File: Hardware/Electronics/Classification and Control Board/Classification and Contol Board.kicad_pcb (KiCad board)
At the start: 2 copper layers, 1 part, among them U1 STM32F407VETx

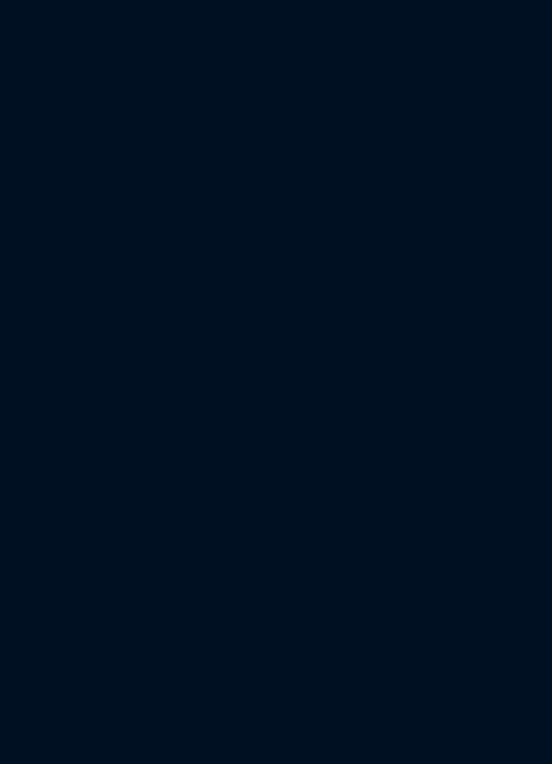
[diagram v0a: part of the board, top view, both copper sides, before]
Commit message: Added SWD programming header
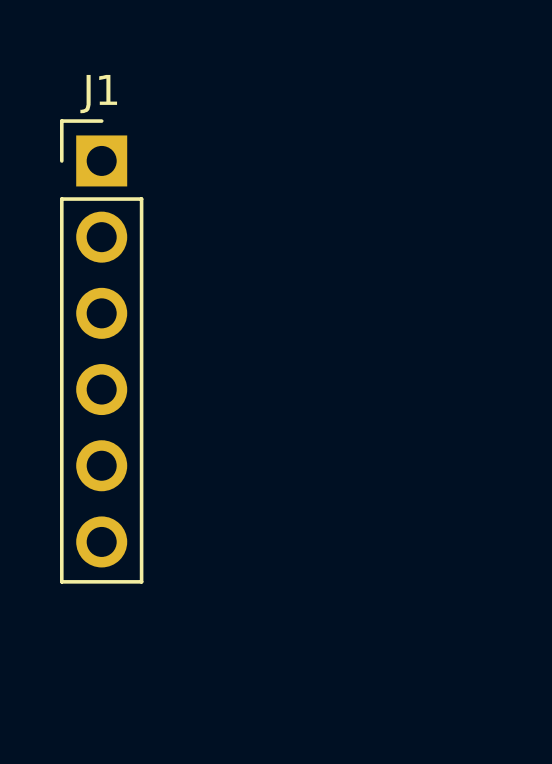
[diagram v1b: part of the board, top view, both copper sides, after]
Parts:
- added J1: Conn_01x06_Male, Connector_PinHeader_2.54mm:PinHeader_1x06_P2.54mm_Vertical, F.Cu at (100.2, 56.7)
- U1: value STM32F407VETx -> STM32F407VGTx
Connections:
- U1 pad 14: Net-(U1-Pad14) -> /NRST
- U1 pad 76: Net-(U1-Pad76) -> /SWCLK
- U1 pad 89: Net-(U1-Pad89) -> /SWO

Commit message: removed some decoupling, started layout
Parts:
- added C1: 100u, Capacitor_SMD:CP_Elec_6.3x7.7, F.Cu at (274.9, 66.3)
- added C10: 100n, Capacitor_SMD:C_0603_1608Metric, F.Cu at (242.5, 34.6)
- added C11: 10n, Capacitor_SMD:C_0603_1608Metric, F.Cu at (244.1, 34.6)
- added C12: 10n, Capacitor_SMD:C_0603_1608Metric, F.Cu at (245.7, 34.6)
- added C13: 0.1u, Capacitor_SMD:C_0603_1608Metric, F.Cu at (249.5, 49.2)
- added C15: 4.7u, Capacitor_SMD:C_0603_1608Metric, F.Cu at (272.9, 56.7)
- added C16: 100n, Capacitor_SMD:C_0603_1608Metric, F.Cu at (240.9, 41.4)
- added C17: 100n, Capacitor_SMD:C_0603_1608Metric, F.Cu at (242.5, 41.4)
- added C18: 10n, Capacitor_SMD:C_0603_1608Metric, F.Cu at (244.0, 41.4)
- added C19: 10n, Capacitor_SMD:C_0603_1608Metric, F.Cu at (245.6, 41.4)
- added C2: 100n, Capacitor_SMD:C_0603_1608Metric, F.Cu at (244.8, 27.1)
- added C20: 10n, Capacitor_SMD:C_0603_1608Metric, F.Cu at (272.9, 55.1)
- added C21: 100n, Capacitor_SMD:C_0603_1608Metric, F.Cu at (255.7, 49.2)
- added C22: 100n, Capacitor_SMD:C_0603_1608Metric, F.Cu at (254.2, 49.2)
- added C23: 10n, Capacitor_SMD:C_0603_1608Metric, F.Cu at (252.6, 49.2)
- added C24: 10n, Capacitor_SMD:C_0603_1608Metric, F.Cu at (251.1, 49.2)
- added C25: 1n, Capacitor_SMD:C_0603_1608Metric, F.Cu at (272.9, 53.6)
- added C26: 100n, Capacitor_SMD:C_0603_1608Metric, F.Cu at (263.9, 52.8)
- added C27: 100n, Capacitor_SMD:C_0603_1608Metric, F.Cu at (263.9, 51.2)
- added C28: 10n, Capacitor_SMD:C_0603_1608Metric, F.Cu at (263.9, 49.7)
- added C29: 10n, Capacitor_SMD:C_0603_1608Metric, F.Cu at (263.9, 48.1)
- added C3: 100n, Capacitor_SMD:C_0603_1608Metric, F.Cu at (244.8, 28.8)
- added C30: 100n, Capacitor_SMD:C_0603_1608Metric, F.Cu at (266.7, 27.2)
- added C31: 100n, Capacitor_SMD:C_0603_1608Metric, F.Cu at (266.7, 28.7)
- added C32: 10n, Capacitor_SMD:C_0603_1608Metric, F.Cu at (266.7, 30.3)
- added C33: 10n, Capacitor_SMD:C_0603_1608Metric, F.Cu at (266.7, 31.8)
- added C34: 10n, Capacitor_SMD:C_0603_1608Metric, F.Cu at (245.2, 50.2)
- added C35: 100n, Capacitor_SMD:C_0603_1608Metric, F.Cu at (249.2, 24.0)
- added C36: 100n, Capacitor_SMD:C_0603_1608Metric, F.Cu at (249.2, 25.6)
- added C37: 10n, Capacitor_SMD:C_0603_1608Metric, F.Cu at (249.2, 27.1)
- added C38: 10n, Capacitor_SMD:C_0603_1608Metric, F.Cu at (249.2, 28.6)
- added C39: 100n, Capacitor_SMD:C_0603_1608Metric, F.Cu at (245.2, 48.6)
- added C4: 10n, Capacitor_SMD:C_0603_1608Metric, F.Cu at (245.0, 32.0)
- added C40: 1n, Capacitor_SMD:C_0603_1608Metric, F.Cu at (270.6, 42.7)
- added C41: 1u, Capacitor_SMD:C_0603_1608Metric, F.Cu at (245.2, 47.1)
- added C46: 10n, Capacitor_SMD:C_0603_1608Metric, F.Cu at (270.6, 41.2)
- added C47: 4.7u, Capacitor_SMD:C_0603_1608Metric, F.Cu at (270.6, 39.6)
- added C48: 10u, Capacitor_SMD:CP_Elec_4x5.4, F.Cu at (271.6, 36.2)
- added C49: 2.2u, Capacitor_SMD:C_0603_1608Metric, F.Cu at (261.6, 49.0)
- added C5: 10n, Capacitor_SMD:C_0603_1608Metric, F.Cu at (244.8, 30.4)
- added C50: 1u, Capacitor_SMD:C_0603_1608Metric, F.Cu at (244.1, 44.5)
- added C51: 2.2u, Capacitor_SMD:C_0603_1608Metric, F.Cu at (266.7, 33.4)
- added C52: 10n, Capacitor_SMD:C_0603_1608Metric, F.Cu at (245.7, 44.5)
- added C53: 100u, Capacitor_SMD:CP_Elec_6.3x7.7, F.Cu at (244.3, 94.6)
- added C54: 100u, Capacitor_SMD:CP_Elec_6.3x7.7, F.Cu at (251.8, 94.5)
- added C55: 10u, Capacitor_SMD:CP_Elec_4x5.4, F.Cu at (258.0, 95.8)
- added C56: 10u, Capacitor_SMD:CP_Elec_4x5.4, F.Cu at (262.9, 95.7)
- added C57: 4.7u, Capacitor_SMD:C_0603_1608Metric, F.Cu at (270.7, 97.5)
- added C60: 4.7u, Capacitor_SMD:C_0603_1608Metric, F.Cu at (37.7, 15.9)
- added C61: 100n, Capacitor_SMD:C_0603_1608Metric, F.Cu at (49.2, 12.4)
- added C62: 100n, Capacitor_SMD:C_0603_1608Metric, F.Cu at (39.2, 15.9)
- added C63: 10n, Capacitor_SMD:C_0603_1608Metric, F.Cu at (47.7, 12.4)
- added C64: 10n, Capacitor_SMD:C_0603_1608Metric, F.Cu at (40.8, 15.9)
- added C65: 10n, Capacitor_SMD:C_0603_1608Metric, F.Cu at (47.7, 9.29)
- added C67: 100n, Capacitor_SMD:C_0603_1608Metric, F.Cu at (49.2, 9.30)
- added C68: 4.7u, Capacitor_SMD:C_0603_1608Metric, F.Cu at (40.8, 20.1)
- added C7: 10u, Capacitor_SMD:CP_Elec_4x5.4, F.Cu at (273.9, 60.0)
- added C70: 100n, Capacitor_SMD:C_0603_1608Metric, F.Cu at (39.3, 20.1)
- added C71: 10n, Capacitor_SMD:C_0603_1608Metric, F.Cu at (37.7, 20.1)
- added C9: 100n, Capacitor_SMD:C_0603_1608Metric, F.Cu at (240.9, 34.6)
- added D1: LTST-C171TBKT, LED_SMD:LED_0805_2012Metric, F.Cu at (-17.4, -14.9)
- added D2: LO R976-PS-1, LED_SMD:LED_0805_2012Metric, F.Cu at (17.1, -25.7)
- added D3: 10V, Diode_SMD:D_SMA, F.Cu at (237.2, 96.6)
- added D4: LED, LED_SMD:LED_0603_1608Metric, F.Cu at (-64.0, -19.9)
- added D5: LED, LED_SMD:LED_0603_1608Metric, F.Cu at (-61.0, -19.9)
- added D6: LED, LED_SMD:LED_0603_1608Metric, F.Cu at (-23.2, -42.0)
- added F1: Fuse, Resistor_THT:R_Axial_Power_L20.0mm_W6.4mm_P25.40mm, F.Cu at (235.2, 85.5)
- added J10: USB_B_Mini, Connector_USB:USB_Micro-B_Wuerth_629105150521, F.Cu at (-76.6, 8.15)
- added J2: Barrel_Jack, Connector_BarrelJack:BarrelJack_CUI_PJ-063AH_Horizontal, F.Cu at (227.5, 85.8)
- added J3: Thumb, Connector_PinHeader_2.54mm:PinHeader_1x03_P2.54mm_Horizontal, F.Cu at (106.2, 92.0)
- added J4: Index, Connector_PinHeader_2.54mm:PinHeader_1x03_P2.54mm_Horizontal, F.Cu at (115.0, 92.0)
- added J5: Middle, Connector_PinHeader_2.54mm:PinHeader_1x03_P2.54mm_Horizontal, F.Cu at (123.7, 92.0)
- added J6: Ring, Connector_PinHeader_2.54mm:PinHeader_1x03_P2.54mm_Horizontal, F.Cu at (136.0, 92.4)
- added J7: Pinky, Connector_PinHeader_2.54mm:PinHeader_1x03_P2.54mm_Horizontal, F.Cu at (135.9, 101.4)
- added J8: Wrist, Connector_PinHeader_2.54mm:PinHeader_1x03_P2.54mm_Horizontal, F.Cu at (135.9, 110.1)
- added J9: HC05, Resonators:HC-05, F.Cu at (80.4, -68.8)
- added LOGO1: SparkerLogo, Sparker:NASA, F.Cu at (-95.3, -20.5)
- added LOGO2: UoNLogo, Sparker:UoN, F.Cu at (-93.0, -1.31)
- added MH1: MountingHole, MountingHole:MountingHole_2.7mm_M2.5, F.Cu at (-34.3, 7.48)
- added MH2: MountingHole, MountingHole:MountingHole_2.7mm_M2.5, F.Cu at (-40.2, 7.48)
- added MH3: MountingHole, MountingHole:MountingHole_2.7mm_M2.5, F.Cu at (-52.4, 8.02)
- added MH4: MountingHole, MountingHole:MountingHole_2.7mm_M2.5, F.Cu at (-46.2, 7.48)
- added Q1: SQ3425EV-T1_GE3, Package_TO_SOT_SMD:TSOT-23-6, F.Cu at (238.2, 92.9)
- added R1: 100k, Resistor_SMD:R_0603_1608Metric, F.Cu at (252.9, 22.5)
- added R10: 50m, Resistor_SMD:R_0603_1608Metric, F.Cu at (132.5, 103.9)
- added R11: 50m, Resistor_SMD:R_0603_1608Metric, F.Cu at (132.5, 112.7)
- added R12: 500k, Resistor_SMD:R_0603_1608Metric, F.Cu at (245.2, 53.3)
- added R13: 100k, Resistor_SMD:R_0603_1608Metric, F.Cu at (245.2, 51.8)
- added R14: 500k, Resistor_SMD:R_0603_1608Metric, F.Cu at (106.5, 94.8)
- added R15: 100k, Resistor_SMD:R_0603_1608Metric, F.Cu at (106.4, 96.4)
- added R16: 500k, Resistor_SMD:R_0603_1608Metric, F.Cu at (115.2, 94.7)
- added R17: 100k, Resistor_SMD:R_0603_1608Metric, F.Cu at (115.2, 96.3)
- added R18: 500k, Resistor_SMD:R_0603_1608Metric, F.Cu at (123.9, 94.7)
- added R19: 100k, Resistor_SMD:R_0603_1608Metric, F.Cu at (123.9, 96.2)
- added R2: 100k, Resistor_SMD:R_0603_1608Metric, F.Cu at (252.9, 20.9)
- added R20: 500k, Resistor_SMD:R_0603_1608Metric, F.Cu at (133.3, 92.7)
- added R21: 100k, Resistor_SMD:R_0603_1608Metric, F.Cu at (131.8, 92.7)
- added R22: 500k, Resistor_SMD:R_0603_1608Metric, F.Cu at (133.3, 101.6)
- added R23: 100k, Resistor_SMD:R_0603_1608Metric, F.Cu at (131.7, 101.6)
- added R24: 500k, Resistor_SMD:R_0603_1608Metric, F.Cu at (133.3, 110.4)
- added R25: 100k, Resistor_SMD:R_0603_1608Metric, F.Cu at (131.8, 110.4)
- added R26: 150, Resistor_SMD:R_0603_1608Metric, F.Cu at (-64.0, -17.0)
- added R27: 150, Resistor_SMD:R_0603_1608Metric, F.Cu at (-60.9, -23.1)
- added R28: 150, Resistor_SMD:R_0603_1608Metric, F.Cu at (-19.0, -41.8)
- added R4: 65R, Resistor_SMD:R_0603_1608Metric, F.Cu at (17.2, -28.4)
- added R5: 33k, Resistor_SMD:R_0603_1608Metric, F.Cu at (234.4, 93.2)
- added R6: 50m, Resistor_SMD:R_0603_1608Metric, F.Cu at (108.8, 95.6)
- added R7: 50m, Resistor_SMD:R_0603_1608Metric, F.Cu at (117.5, 95.5)
- added R8: 50m, Resistor_SMD:R_0603_1608Metric, F.Cu at (126.2, 95.5)
- added R9: 50m, Resistor_SMD:R_0603_1608Metric, F.Cu at (132.5, 95.0)
- added SW1: SW_Push, Switches:1825910-6, F.Cu at (235.0, 52.0)
- added SW2: SW_DIP_x02, Switches:DIP-Switch_01x02, F.Cu at (253.1, 25.0)
- added SW3: BT Enable, Switches:DIP-Switch_01x02, F.Cu at (32.8, 13.1)
- added U2: STM32F407VGTx, Package_QFP:LQFP-100_14x14mm_P0.5mm, F.Cu at (256.1, 38.4)
- added U3: MCP1755T-5002E_SOT223-5, Package_TO_SOT_SMD:SOT-223-6, F.Cu at (46.1, 18.0)
- added U4: FT232RL, Package_SO:SSOP-28_5.3x10.2mm_P0.65mm, F.Cu at (42.0, 7.48)
- added Y1: 12MHz, Resonators:CSTNE12M0GH5L000R0, F.Cu at (245.1, 38.2)
- J1: value Conn_01x06_Male -> SWD Header
- U1: value STM32F407VGTx -> LDL1117S33R; footprint Package_QFP:LQFP-100_14x14mm_P0.5mm -> Package_TO_SOT_SMD:SOT-223-3_TabPin2
- moved U1 136.8 mm to (269.8, 48.2), turned to 90 degrees
- moved J1 131.5 mm to (231.6, 51.1), turned to 180 degrees
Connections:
- J1 pad 1: /3V3 -> /STM32F407VGTx/3V3
- J1 pad 2: /SWCLK -> /STM32F407VGTx/SWCLK
- J1 pad 4: /SWDIO -> /STM32F407VGTx/SWDIO
- J1 pad 5: /NRST -> /STM32F407VGTx/NRST
- J1 pad 6: /SWO -> /STM32F407VGTx/SWO
- U1 pad 1: Net-(U1-Pad1) -> /GND
- U1 pad 2: Net-(U1-Pad2) -> /STM32F407VGTx/3V3
- U1 pad 3: Net-(U1-Pad3) -> /V+
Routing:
- net /STM32F407VGTx/3V3: track 0.00 -> 19.3 mm
- net Net-(U2-Pad12): track 0.00 -> 3.53 mm
- net Net-(U2-Pad13): track 0.00 -> 3.49 mm

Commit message: About to start routing
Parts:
- removed C1, C54: 100u, Capacitor_SMD:CP_Elec_6.3x7.7
- removed C10, C17, C22, C27, C3, C31, C36: 100n, Capacitor_SMD:C_0603_1608Metric
- removed C12, C19, C24, C29, C33, C38, C5: 10n, Capacitor_SMD:C_0603_1608Metric
- removed C48, C56, C7: 10u, Capacitor_SMD:CP_Elec_4x5.4
- removed D4, D5: LED, LED_SMD:LED_0603_1608Metric
- removed F1: Fuse, Resistor_THT:R_Axial_Power_L20.0mm_W6.4mm_P25.40mm
- removed MH4: MountingHole, MountingHole:MountingHole_2.7mm_M2.5
- removed R26, R27: 150, Resistor_SMD:R_0603_1608Metric
- J9: moved to B.Cu
- LOGO1: footprint Sparker:NASA -> Sparker:NASA_small
- moved LOGO1 291.0 mm to (158.8, 121.3)
- moved LOGO2 257.8 mm to (156.2, 64.9)
- moved J10 247.6 mm to (144.9, 118.8)
- moved D6 239.4 mm to (157.9, 114.6)
- moved R28 234.9 mm to (158.7, 111.8), turned to 90 degrees
- moved MH3 224.2 mm to (164.6, 64.5)
- moved MH2 204.5 mm to (131.0, 119.2)
- moved J9 199.7 mm to (152.4, 117.4), turned to 270 degrees
- moved D1 186.8 mm to (126.7, 104.0), turned to 90 degrees
- moved MH1 182.4 mm to (126.5, 93.6)
- moved D2 168.5 mm to (124.6, 104.0), turned to 90 degrees
- moved R4 167.9 mm to (124.5, 100.7), turned to 270 degrees
- moved SW3 155.8 mm to (152.3, 113.2)
- moved C57 155.0 mm to (116.1, 87.1), turned to 90 degrees
- moved C60 154.2 mm to (165.2, 102.6), turned to 0 degrees
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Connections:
- D1 pad 2: Net-(D1-Pad2) -> /STM32F407VGTx/3V3
- J2 pad 1: Net-(F1-Pad2) -> Net-(J2-Pad1)
- Q1 pad 1: Net-(F1-Pad1) -> Net-(J2-Pad1)
- Q1 pad 2: Net-(F1-Pad1) -> Net-(J2-Pad1)
- Q1 pad 5: Net-(F1-Pad1) -> Net-(J2-Pad1)
- Q1 pad 6: Net-(F1-Pad1) -> Net-(J2-Pad1)
- U2 pad 40: Net-(D1-Pad2) -> Net-(U2-Pad40)
- U4 pad 5: /Communications/RX -> Net-(U4-Pad5)
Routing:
- net /Communications/D-: track 0.00 -> 34.8 mm
- net /Communications/D+: track 0.00 -> 34.1 mm
- net /STM32F407VGTx/3V3: track 19.3 -> 18.7 mm
- added copper zone on B.Cu, net /GND
- added copper zone on F.Cu, net /GND
- added copper zone on In1.Cu, net /GND
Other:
- board outline added: 53.9 x 62.3 mm
- copper layers 2 -> 4

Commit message: Started Routing
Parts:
- moved C13 12.2 mm to (123.0, 84.9), turned to 180 degrees
- moved SW3 9.23 mm to (154.9, 104.3), turned to 270 degrees
- moved C67 5.59 mm to (164.9, 86.7), turned to 180 degrees
- moved R5 4.70 mm to (121.4, 102.8)
- moved Q1 1.86 mm to (121.6, 105.9)
- moved D3 0.99 mm to (118.0, 104.6), turned to 90 degrees
- moved J9 0.61 mm to (152.4, 118.0)
- moved R14 0.43 mm to (117.6, 74.5)
- moved R15 0.43 mm to (117.6, 76.1)
- moved R6 0.43 mm to (119.9, 75.3)
- moved C65 0.05 mm to (167.2, 94.7)
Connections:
- J9 pad 2: /Communications/+5V -> Net-(J9-Pad2)
- J9 pad 3: /GND -> Net-(J9-Pad3)
- J9 pad 4: Net-(J9-Pad4) -> /GND
- J9 pad 5: Net-(J9-Pad5) -> /Communications/+5V
- SW3 pad 3: Net-(J9-Pad5) -> Net-(J9-Pad2)
- SW3 pad 4: Net-(J9-Pad4) -> Net-(J9-Pad3)
- U4 pad 5: Net-(U4-Pad5) -> /Communications/RX
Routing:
- net /Communications/TX: track 0.00 -> 57.2 mm, vias 0 -> 2
- net /Communications/RX: track 0.00 -> 50.8 mm, vias 0 -> 2
- net /STM32F407VGTx/3V3: track 18.7 -> 60.9 mm, vias 0 -> 1
- net /V+: track 0.00 -> 35.8 mm
- net /Communications/+5V: track 0.00 -> 31.8 mm, vias 0 -> 1
- net /STM32F407VGTx/BOOT1: track 0.00 -> 25.0 mm, vias 0 -> 2
- net Net-(C61-Pad1): track 0.00 -> 21.0 mm, vias 0 -> 2
- net /STM32F407VGTx/NRST: track 0.00 -> 19.3 mm, vias 0 -> 1
- net Net-(R4-Pad1): track 0.00 -> 10.7 mm
- net /STM32F407VGTx/BOOT0: track 0.00 -> 7.79 mm
- net Net-(J2-Pad1): track 0.00 -> 7.37 mm
- net Net-(J9-Pad2): track 0.00 -> 6.50 mm
- net /Control/FB_REF: track 0.00 -> 6.35 mm
- net Net-(J9-Pad3): track 0.00 -> 6.20 mm
- net Net-(D3-Pad2): track 0.00 -> 4.53 mm
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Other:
- net class 0.5mm added: clearance 0.2, trace_width 0.5, via_dia 0.8, via_drill 0.4
- net class 1mm added: clearance 0.2, trace_width 1, via_dia 0.8, via_drill 0.4

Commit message: Most signals routed, working on power now
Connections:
- U2 pad 15: /Control/FB1 -> /Control/FB4
- U2 pad 16: /Control/FB2 -> /Control/FB3
- U2 pad 17: /Control/FB3 -> /Control/FB2
- U2 pad 18: /Control/FB4 -> /Control/FB1
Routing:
- net /STM32F407VGTx/NRST: track 19.3 -> 57.2 mm, vias 1 -> 2
- net /STM32F407VGTx/PWM5: track 0.00 -> 36.2 mm
- net /Control/FB5: track 1.55 -> 36.8 mm, vias 0 -> 2
- net /Control/FB1: track 1.58 -> 35.6 mm, vias 0 -> 2
- net /Control/FB6: track 1.54 -> 32.7 mm, vias 0 -> 2
- net /STM32F407VGTx/PWM4: track 0.00 -> 30.6 mm, vias 0 -> 1
- net /STM32F407VGTx/SWO: track 0.00 -> 28.7 mm, vias 0 -> 1
- net /STM32F407VGTx/PWM1: track 0.00 -> 26.8 mm, vias 0 -> 1
- net /STM32F407VGTx/PWM3: track 0.00 -> 26.1 mm, vias 0 -> 1
- net /STM32F407VGTx/PWM2: track 0.00 -> 24.8 mm, vias 0 -> 1
- net /Control/FB2: track 1.54 -> 26.0 mm, vias 0 -> 2
- net /STM32F407VGTx/SWCLK: track 0.00 -> 19.4 mm, vias 0 -> 1
- net /STM32F407VGTx/SWDIO: track 0.00 -> 18.9 mm, vias 0 -> 1
- net /Control/FB3: track 1.54 -> 16.7 mm, vias 0 -> 2
- net /Control/FB4: track 1.54 -> 16.3 mm, vias 0 -> 2
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
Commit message: about to grid vias
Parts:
- moved C61 3.80 mm to (166.3, 100.9)
- moved C63 3.80 mm to (166.3, 99.3)
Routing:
- net /STM32F407VGTx/3V3: track 60.9 -> 81.6 mm, vias 1 -> 9
- net /V+: track 35.8 -> 52.7 mm, vias 0 -> 10
- net Net-(C61-Pad1): track 21.0 -> 19.2 mm
- net /Communications/+5V: track 31.8 -> 33.4 mm, vias 1 -> 2
- added copper zone on In2.Cu, net /Communications/+5V
- added copper zone on In2.Cu, net /STM32F407VGTx/3V3
- added copper zone on In2.Cu, net /V+

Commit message: Routing done
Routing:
- net /GND: track 0.00 -> 20.6 mm, vias 0 -> 165
- net /STM32F407VGTx/PWM6: track 12.9 -> 24.8 mm
- net /STM32F407VGTx/NRST: track 57.2 -> 62.0 mm
- net /STM32F407VGTx/3V3: track 81.6 -> 86.1 mm, vias 9 -> 10
- net /Control/FB4: track 16.3 -> 19.2 mm
- net /Control/FB5: track 36.8 -> 37.6 mm

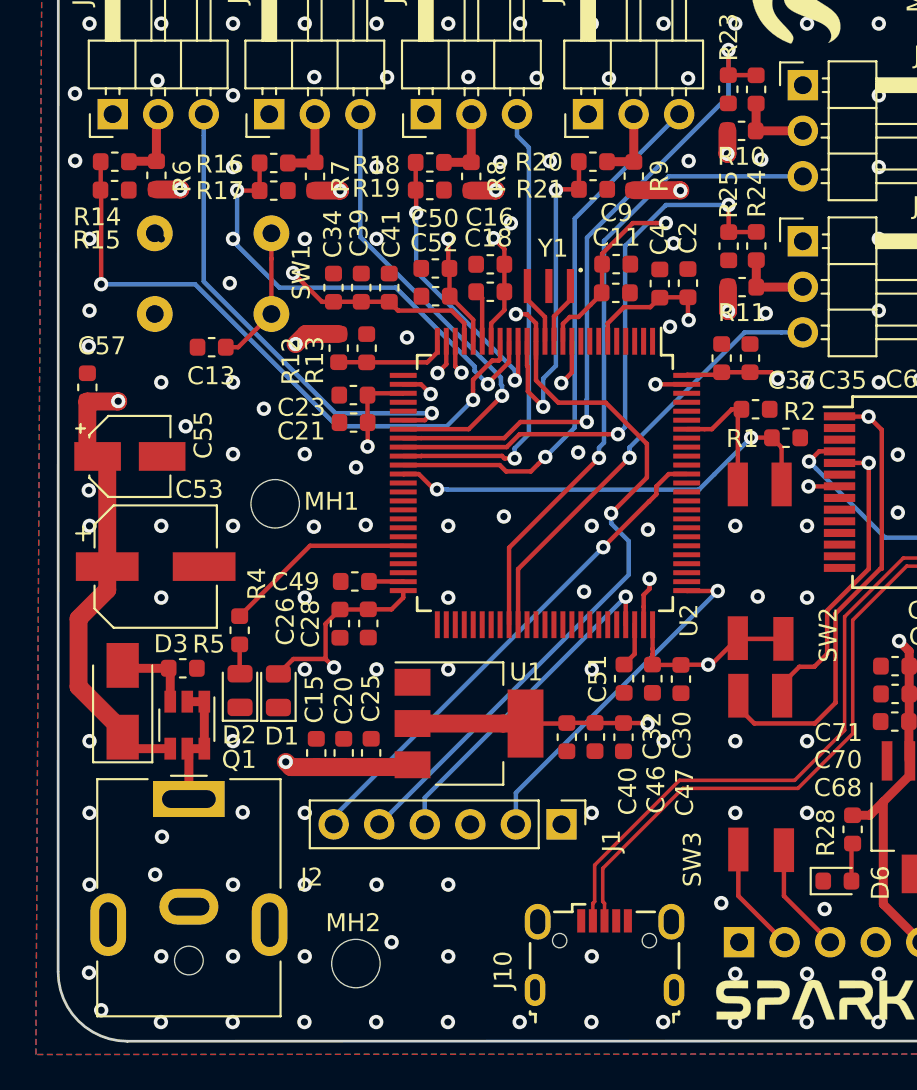
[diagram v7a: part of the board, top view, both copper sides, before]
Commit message: Flipped the DC connector
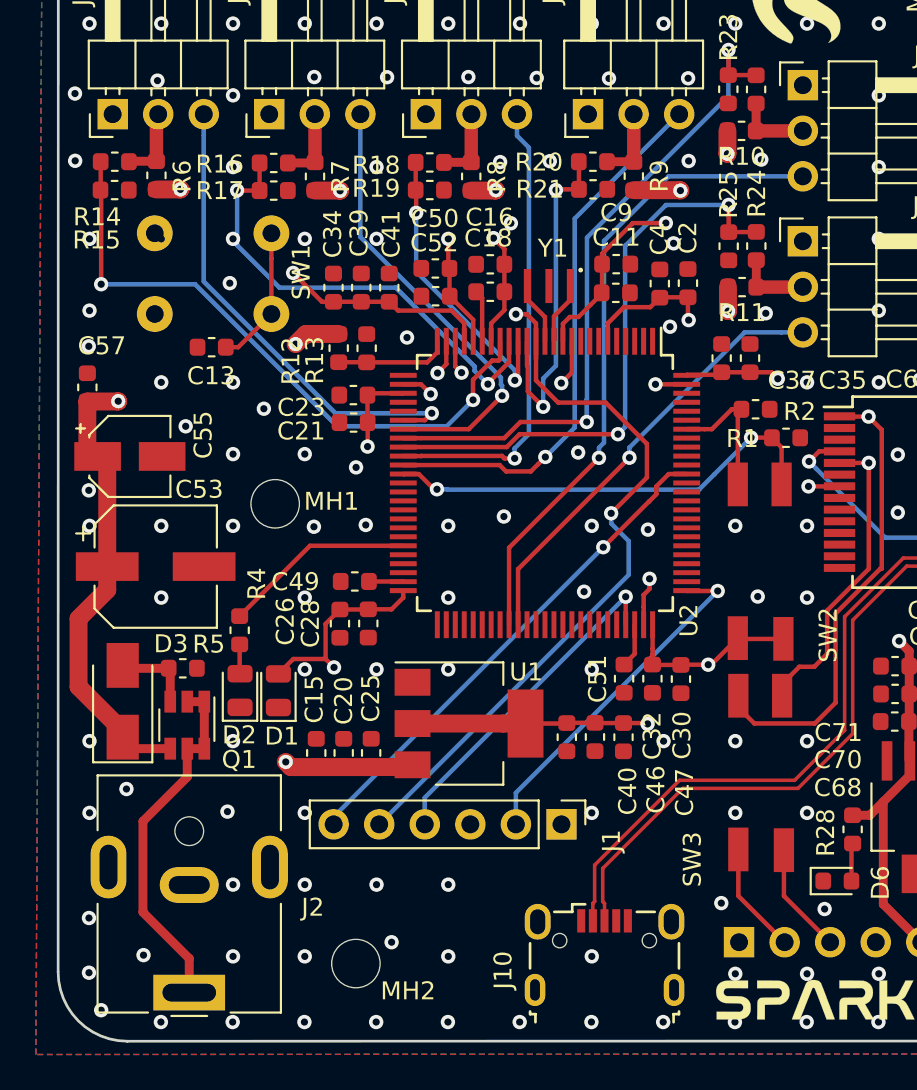
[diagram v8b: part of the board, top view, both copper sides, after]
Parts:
- moved J2 10.8 mm to (121.7, 120.8), turned to 180 degrees
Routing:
- net Net-(J2-Pad1): track 7.37 -> 20.3 mm
- net /GND: vias 165 -> 164
